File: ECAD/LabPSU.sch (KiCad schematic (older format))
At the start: 3 parts, among them J1 PWR

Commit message: work on things
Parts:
- removed D?: D_Bridge_+-AA, symbol Device:D_Bridge_+-AA
- added C? (x3): CP, symbol Device:CP
- added D1: FULL BRIDGE RECTIFIER, symbol Device:D_Bridge_+AA-
- added U?: BD9G341EFJ, Package_SO:HTSOP-8-1EP_3.9x4.9mm_P1.27mm_EP2.4x3.2mm_ThermalVias, symbol Regulator_Switching:BD9G341EFJ
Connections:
- net labels added: Earth, VDC
- wire segments 6 -> 15
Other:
- moved on the sheet: U?
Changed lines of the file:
@@
 	-1   0    0    1
-$EndComp
-$Comp
-L power:GND #PWR?
-U 1 1 61BA3EE6
-P 1950 2950
-F 0 "#PWR?" H 1950 2700 50  0001 C CNN
-F 1 "GND" H 1955 2777 50  0000 C CNN
-F 2 "" H 1950 2950 50  0001 C CNN
-F 3 "" H 1950 2950 50  0001 C CNN
-	1    1950 2950
-	1    0    0    -1
 $EndComp
 Wire Wire Line
 	1950 2950 1950 2850
-$Comp
-L power:VAC #PWR?
-U 1 1 61BA312C
-P 1950 2650
-F 0 "#PWR?" H 1950 2550 50  0001 C CNN
-F 1 "VAC" H 1950 2925 50  0000 C CNN
-F 2 "" H 1950 2650 50  0001 C CNN
-F 3 "" H 1950 2650 50  0001 C CNN
-	1    1950 2650
-	1    0    0    -1
-$EndComp
 Wire Wire Line
 	1900 2650 1950 2650
-$Comp
-L Device:D_Bridge_+-AA D?
-U 1 1 61BA4E82
-P 2700 2750
-F 0 "D?" H 3044 2796 50  0000 L CNN
-F 1 "D_Bridge_+-AA" H 3044 2705 50  0000 L CNN
-F 2 "" H 2700 2750 50  0001 C CNN
-F 3 "~" H 2700 2750 50  0001 C CNN
-	1    2700 2750
-	1    0    0    -1
-$EndComp
 Wire Wire Line
 	1900 2750 1950 2750
 Wire Wire Line
 	1950 2750 1950 2650
-Connection ~ 1950 2650
 Wire Wire Line
 	1950 2950 1900 2950
-Connection ~ 1950 2950
 Wire Wire Line
 	1900 2850 1950 2850
@@
 L Regulator_Switching:LM5118MH U?
 U 1 1 61BB989F
-P 4600 3400
-F 0 "U?" H 4600 4167 50  0000 C CNN
-F 1 "LM5118MH" H 4600 4076 50  0000 C CNN
-F 2 "Package_SO:Texas_PWP0020A" H 5300 4050 50  0001 L CNN
-F 3 "https://www.ti.com/lit/ds/symlink/lm5118.pdf" H 6600 2950 50  0001 C CNN
-	1    4600 3400
+P 4550 2500
+F 0 "U?" H 4550 3267 50  0000 C CNN
+F 1 "LM5118MH" H 4550 3176 50  0000 C CNN
+F 2 "Package_SO:Texas_PWP0020A" H 5250 3150 50  0001 L CNN
+F 3 "https://www.ti.com/lit/ds/symlink/lm5118.pdf" H 6550 2050 50  0001 C CNN
+	1    4550 2500
 	1    0    0    -1
 $EndComp
+$Comp
+L Regulator_Switching:BD9G341EFJ U?
+U 1 1 61BCA3CD
+P 4550 4350
+F 0 "U?" H 4550 5031 50  0000 C CNN
+F 1 "BD9G341EFJ" H 4550 4940 50  0000 C CNN
+F 2 "Package_SO:HTSOP-8-1EP_3.9x4.9mm_P1.27mm_EP2.4x3.2mm_ThermalVias" H 4650 3900 50  0001 L CNN
+F 3 "https://media.digikey.com/pdf/Data%20Sheets/Rohm%20PDFs/BD9G341EFJ.pdf" H 4550 4350 50  0001 C CNN
+	1    4550 4350
+	1    0    0    -1
+$EndComp
+$Comp
+L Device:D_Bridge_+AA- D1
+U 1 1 61BCBD61
+P 2600 2800
+F 0 "D1" H 2944 2846 50  0000 L CNN
+F 1 "FULL BRIDGE RECTIFIER" H 2150 2350 50  0000 L CNN
+F 2 "" H 2600 2800 50  0001 C CNN
+F 3 "~" H 2600 2800 50  0001 C CNN
+	1    2600 2800
+	1    0    0    -1
+$EndComp
+$Comp
+L power:VAC #PWR?
+U 1 1 61BCE152
+P 2150 2500
+F 0 "#PWR?" H 2150 2400 50  0001 C CNN
+F 1 "VAC" H 2150 2775 50  0000 C CNN
+F 2 "" H 2150 2500 50  0001 C CNN
+F 3 "" H 2150 2500 50  0001 C CNN
+	1    2150 2500
+	1    0    0    -1
+$EndComp
+Wire Wire Line
+	1950 2650 1950 2500
+Wire Wire Line
+	1950 2500 2150 2500
+Connection ~ 1950 2650
+Connection ~ 2150 2500
+Wire Wire Line
+	2150 2500 2600 2500
+Wire Wire Line
+	2600 3100 2150 3100
+Wire Wire Line
+	1950 3100 1950 2950
+Connection ~ 1950 2950
+$Comp
+L power:Earth #PWR?
+U 1 1 61BCF17A
+P 2150 3100
+F 0 "#PWR?" H 2150 2850 50  0001 C CNN
+F 1 "Earth" H 2150 2950 50  0001 C CNN
+F 2 "" H 2150 3100 50  0001 C CNN
+F 3 "~" H 2150 3100 50  0001 C CNN
+	1    2150 3100
+	1    0    0    -1
+$EndComp
+Connection ~ 2150 3100
+Wire Wire Line
+	2150 3100 1950 3100
+Wire Wire Line
+	2300 2800 2300 3200
+Wire Wire Line
+	2300 3200 3200 3200
+Wire Wire Line
+	2900 2800 3200 2800
+$Comp
+L power:VDC #PWR?
+U 1 1 61BD02AF
+P 3200 2800
+F 0 "#PWR?" H 3200 2700 50  0001 C CNN
+F 1 "VDC" H 3215 2973 50  0000 C CNN
+F 2 "" H 3200 2800 50  0001 C CNN
+F 3 "" H 3200 2800 50  0001 C CNN
+	1    3200 2800
+	1    0    0    -1
+$EndComp
+$Comp
+L power:GND #PWR?
+U 1 1 61BD0846
+P 3200 3200
+F 0 "#PWR?" H 3200 2950 50  0001 C CNN
+F 1 "GND" H 3205 3027 50  0000 C CNN
+F 2 "" H 3200 3200 50  0001 C CNN
+F 3 "" H 3200 3200 50  0001 C CNN
+	1    3200 3200
+	1    0    0    -1
+$EndComp
+$Comp
+L Device:CP C?
+U 1 1 61BD0AE5
+P 3000 3000
+F 0 "C?" H 3118 3046 50  0000 L CNN
+F 1 "CP" H 3118 2955 50  0000 L CNN
+F 2 "" H 3038 2850 50  0001 C CNN
+F 3 "~" H 3000 3000 50  0001 C CNN
+	1    3000 3000
+	1    0    0    -1
+$EndComp
+$Comp
+L Device:CP C?
+U 1 1 61BD13FA
+P 3350 3000
+F 0 "C?" H 3468 3046 50  0000 L CNN
+F 1 "CP" H 3468 2955 50  0000 L CNN
+F 2 "" H 3388 2850 50  0001 C CNN
+F 3 "~" H 3350 3000 50  0001 C CNN
+	1    3350 3000
+	1    0    0    -1
+$EndComp
+$Comp
+L Device:CP C?
+U 1 1 61BD178F
+P 3700 3000
+F 0 "C?" H 3818 3046 50  0000 L CNN
+F 1 "CP" H 3818 2955 50  0000 L CNN
+F 2 "" H 3738 2850 50  0001 C CNN
+F 3 "~" H 3700 3000 50  0001 C CNN
+	1    3700 3000
+	1    0    0    -1
+$EndComp

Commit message: Decided to remove AC/DC rectification
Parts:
- removed C? (x3): CP, symbol Device:CP
- removed D1: FULL BRIDGE RECTIFIER, symbol Device:D_Bridge_+AA-
- removed J1: PWR, symbol Connector:Screw_Terminal_01x04
- removed U?: BD9G341EFJ, Package_SO:HTSOP-8-1EP_3.9x4.9mm_P1.27mm_EP2.4x3.2mm_ThermalVias, symbol Regulator_Switching:BD9G341EFJ
- added C? (x5): 4.7uF, symbol Device:C
- added C?: 0.1uF, symbol Device:C
- added J1: PWR, symbol Connector:Screw_Terminal_01x02
- added R?: 1M, symbol Device:R
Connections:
- net labels added: VBUS
- net labels removed: Earth, VAC, VDC
- wire segments 15 -> 22
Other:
- note added: "DC Constant Regulated Input"
- note added: "Variable regulator"
- moved on the sheet: U?

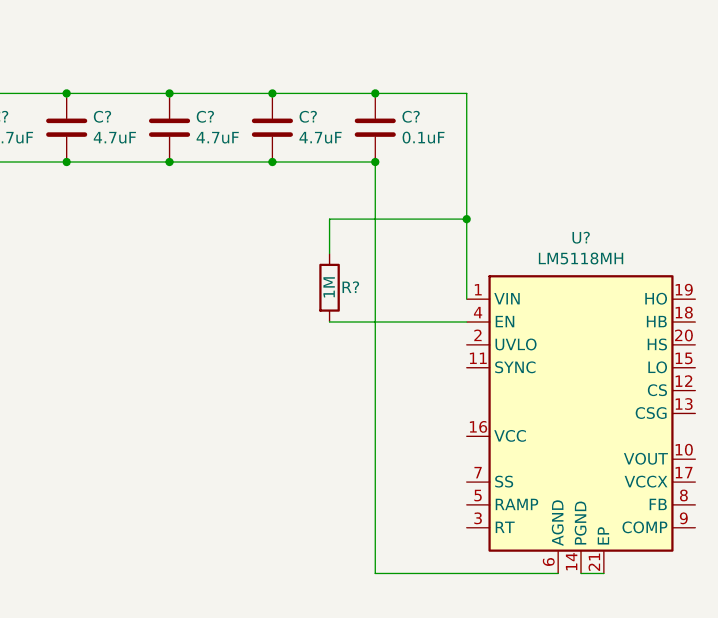
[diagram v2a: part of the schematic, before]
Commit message: add some extra circuitry to lm5118
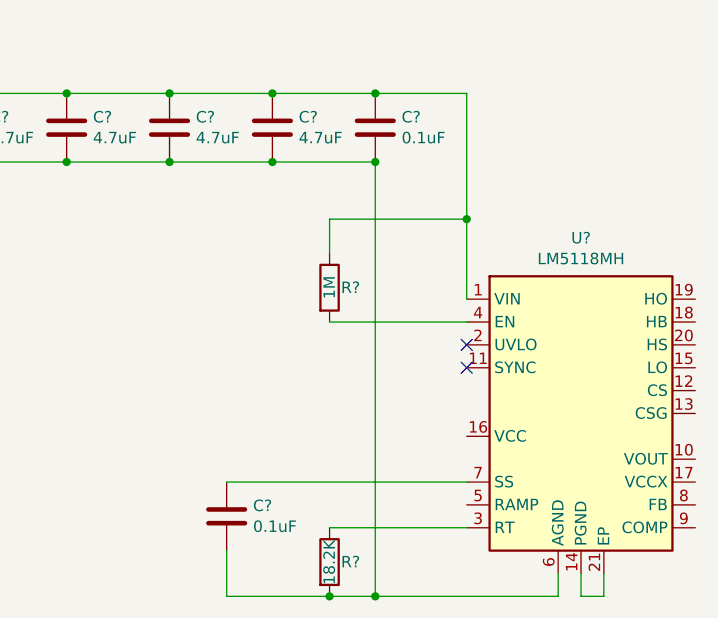
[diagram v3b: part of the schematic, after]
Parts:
- added C?: 0.1uF, symbol Device:C
- added R?: 18.2K, symbol Device:R
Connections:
- net at U?.3 (RT): now also R?.1
- net at C?.2, C?.2, C?.2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: now also C?.2, R?.2
- net at U?.7 (SS): now also C?.1
- no-connect marks 0 -> 2
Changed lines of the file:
@@
 Connection ~ 4200 2050
 Wire Wire Line
-	4650 3850 5450 3850
-Wire Wire Line
-	5550 3850 5650 3850
+	4650 3950 5450 3950
 $Comp
 L Regulator_Switching:LM5118MH U?
@@
 	1    0    0    -1
 $EndComp
-Wire Wire Line
-	4650 2050 4650 3850
 Connection ~ 4650 2050
 Wire Wire Line
@@
 Text Notes 5200 1300 0    50   ~ 0
 Variable regulator
+$Comp
+L Device:R R?
+U 1 1 61C0F85E
+P 4450 3800
+F 0 "R?" H 4500 3800 50  0000 L CNN
+F 1 "18.2K" V 4450 3700 50  0000 L CNN
+F 2 "" V 4380 3800 50  0001 C CNN
+F 3 "~" H 4450 3800 50  0001 C CNN
+	1    4450 3800
+	1    0    0    -1
+$EndComp
+Wire Wire Line
+	4450 3650 5050 3650
+Wire Wire Line
+	5450 3950 5450 3850
+Wire Wire Line
+	4650 2050 4650 3950
+Wire Wire Line
+	4450 3950 4650 3950
+Connection ~ 4650 3950
+Wire Wire Line
+	5550 3850 5550 3950
+Wire Wire Line
+	5550 3950 5650 3950
+Wire Wire Line
+	5650 3950 5650 3850
+$Comp
+L Device:C C?
+U 1 1 61C13AAB
+P 4000 3600
+F 0 "C?" H 4115 3646 50  0000 L CNN
+F 1 "0.1uF" H 4115 3555 50  0000 L CNN
+F 2 "" H 4038 3450 50  0001 C CNN
+F 3 "~" H 4000 3600 50  0001 C CNN
+	1    4000 3600
+	1    0    0    -1
+$EndComp
+Wire Wire Line
+	4000 3450 5050 3450
+Wire Wire Line
+	4000 3750 4000 3950
+Wire Wire Line
+	4000 3950 4450 3950
+Connection ~ 4450 3950
+NoConn ~ 5050 2950
+NoConn ~ 5050 2850
 $EndSCHEMATC

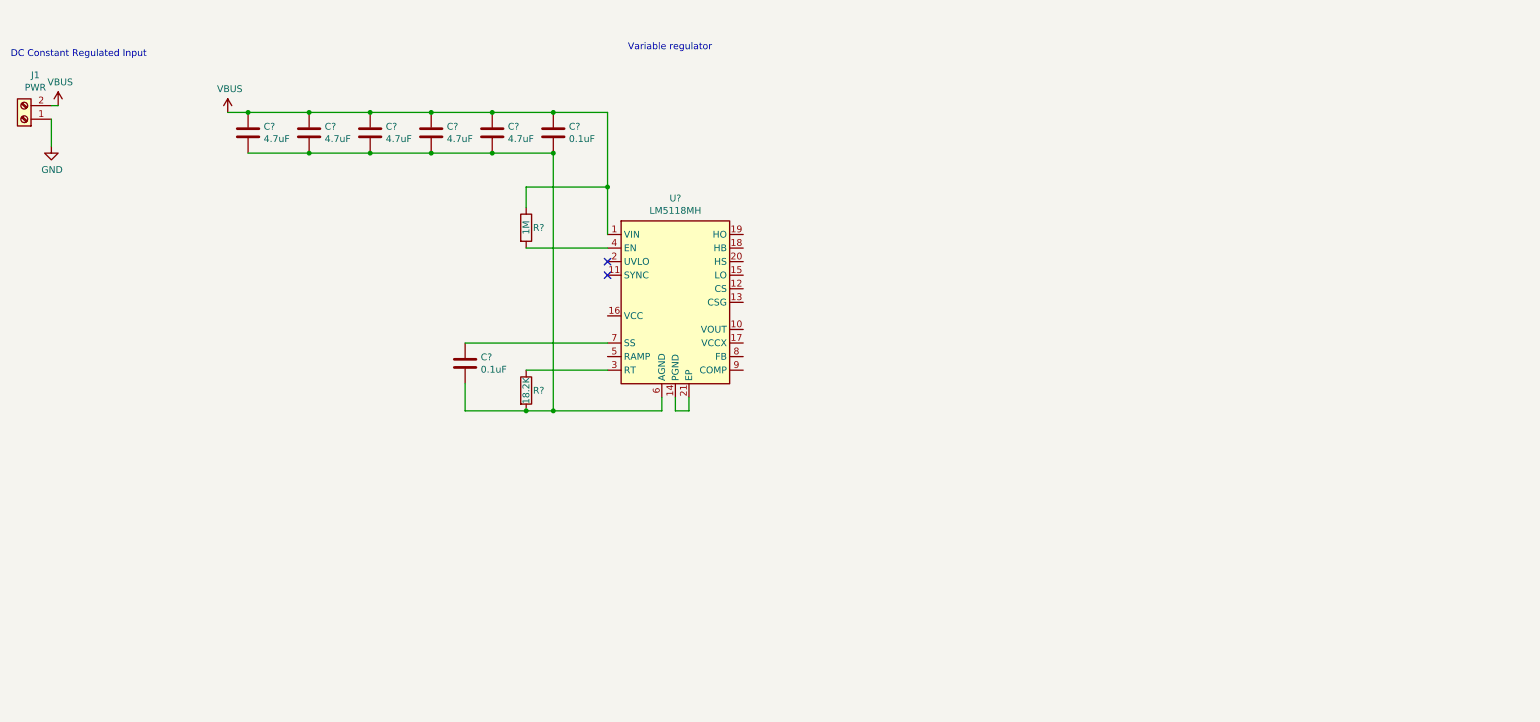
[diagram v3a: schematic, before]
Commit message: Finish adding lm5118 components, yet to calculate values
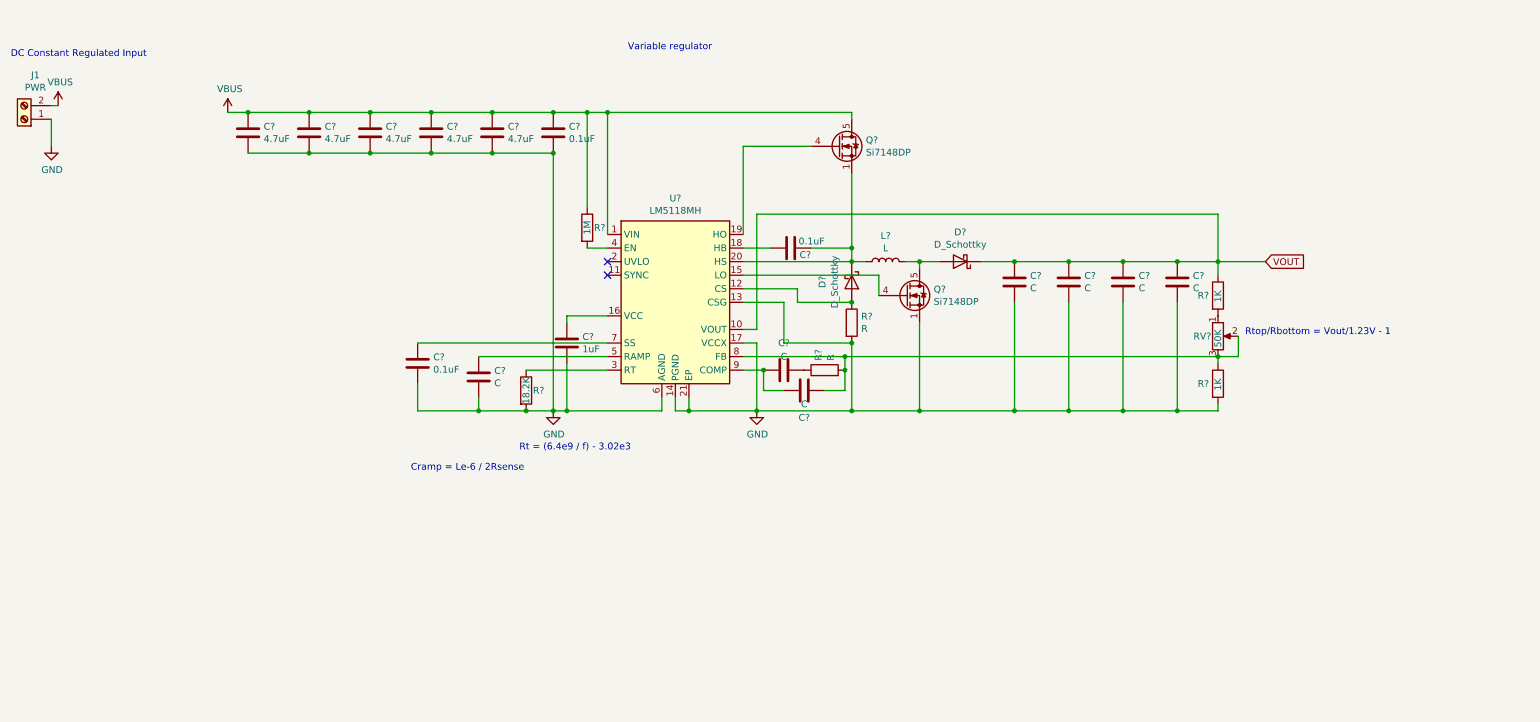
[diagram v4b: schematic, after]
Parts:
- added C? (x7): C, symbol Device:C
- added C?: 1uF, symbol Device:C
- added C?: 0.1uF, symbol Device:C
- added D? (x2): D_Schottky, symbol Device:D_Schottky
- added L?: L, symbol Device:L
- added Q? (x2): Si7148DP, Package_SO:PowerPAK_SO-8_Single, symbol Transistor_FET:Si7336ADP
- added R? (x2): R, symbol Device:R
- added R? (x2): 1K, symbol Device:R
- added RV?: 50K, symbol Device:R_POT
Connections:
- net GND: now also C?.2, C?.2, C?.2, C?.2, C?.2, C?.2, C?.2, R?.2, U?.13 (CSG), U?.14 (PGND), U?.17 (VCCX), U?.21 (EP), U?.6 (AGND), C?.2, C?.2, C?.2, C?.2, C?.2, C?.2, Q?.1 (S), Q?.2 (S), Q?.3 (S), R?.2, R?.2
- net VBUS: now also Q?.5 (D)
- net VOUT: now reaches U?.10 (VOUT)
- net VOUT: now also C?.1, C?.1, C?.1, C?.1, D?.1 (K), R?.1
- net at U?.12 (CS): now also D?.2 (A), R?.1
- net at U?.15 (LO): now also Q?.4 (G)
- net at U?.16 (VCC): now also C?.1
- net at U?.18 (HB): now also C?.1
- net at U?.19 (HO): now also Q?.4 (G)
- net at U?.20 (HS): now also C?.2, D?.1 (K), L?.1, Q?.1 (S), Q?.2 (S), Q?.3 (S)
- net at U?.5 (RAMP): now also C?.1
- net at U?.8 (FB): now also C?.1, R?.1, R?.2, RV?.2, RV?.3
- net at U?.9 (COMP): now also C?.2, C?.2
- new net: D?.2 (A), L?.2, Q?.5 (D)
- new net: C?.1, R?.1
- new net: R?.2, RV?.1
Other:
- note added: "Cramp = Le-6 / 2Rsense"
- note added: "Rt = (6.4e9 / f) - 3.02e3"
- note added: "Rtop/Rbottom = Vout/1.23V - 1"
- moved on the sheet: C?, R?

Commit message: add fixed buck regulator
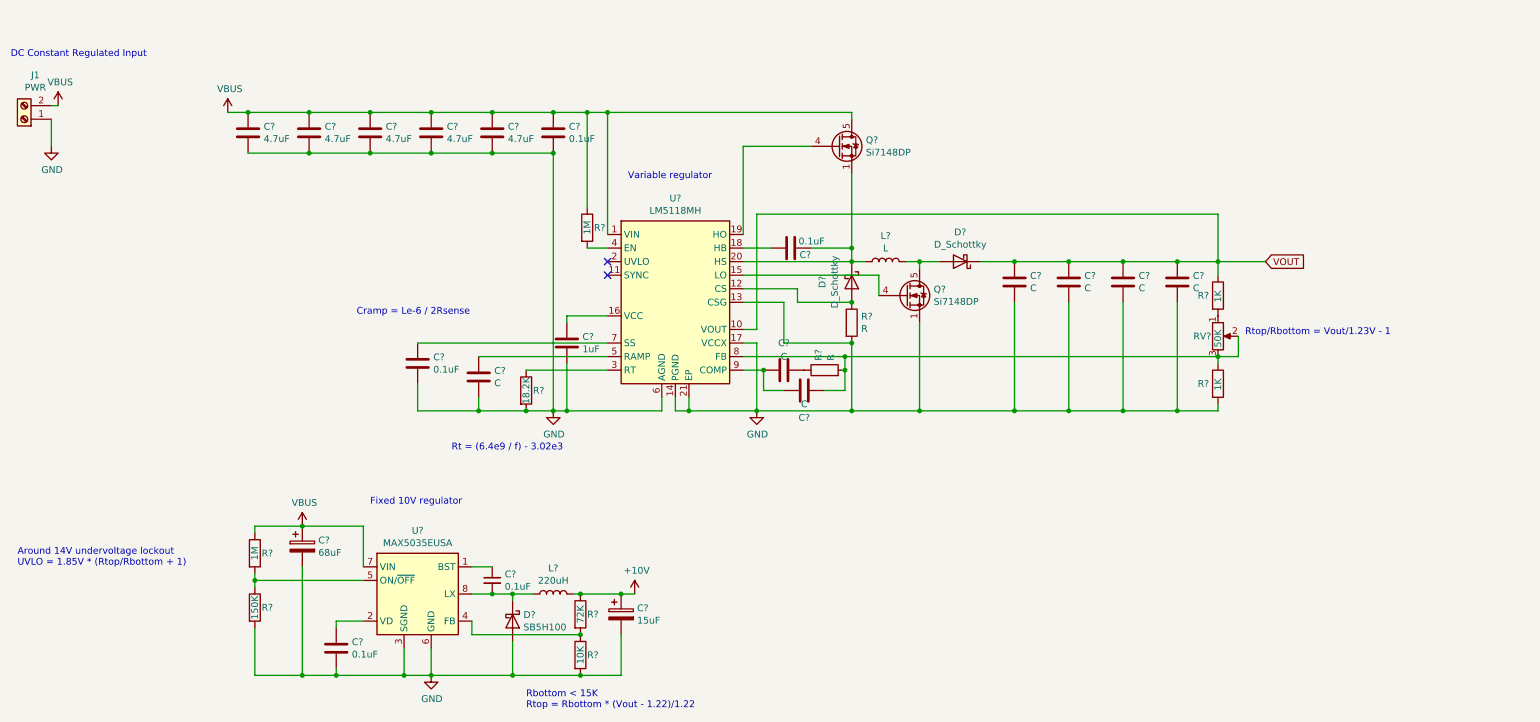
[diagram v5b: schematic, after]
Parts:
- added C?: 68uF, symbol Device:CP
- added C?: 0.1uF, symbol Device:C
- added C?: 0.1uF, symbol Device:C_Small
- added C?: 15uF, symbol Device:CP
- added D?: SB5H100, symbol Device:D_Schottky
- added L?: 220uH, symbol Device:L
- added R?: 150K, symbol Device:R
- added R?: 1M, symbol Device:R
- added R?: 72K, symbol Device:R
- added R?: 10K, symbol Device:R
- added U?: MAX5035EUSA, Package_SO:SOIC-8_3.9x4.9mm_P1.27mm, symbol Regulator_Switching:MAX5035EUSA
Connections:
- net GND: now also C?.2, C?.2, C?.2, D?.2 (A), R?.2, R?.2, U?.3 (SGND), U?.6 (GND)
- net VBUS: now also C?.1, R?.1, U?.7 (VIN)
- new net: C?.1, U?.1 (BST)
- new net: C?.1, U?.2 (VD)
- new net: R?.1, R?.2, U?.4 (FB)
- new net: R?.1, R?.2, U?.5 (ON/~OFF~)
- new net: C?.2, D?.1 (K), L?.1, U?.8 (LX)
- new net +10V: C?.1, L?.2, R?.1
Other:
- note added: "Around 14V undervoltage lockout\nUVLO = 1.85V * (Rtop/Rbottom + 1)"
- note added: "Fixed 10V regulator"
- note added: "Rbottom < 15K\nRtop = Rbottom * (Vout - 1.22)/1.22"

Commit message: end of day commit
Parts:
- added R?: 10m, symbol Device:R
- added U?: LT6106, Package_TO_SOT_SMD:SOT-23-5, symbol Amplifier_Current:LT6106
- added U?: AD5272BRM, Package_SO:MSOP-10_3x3mm_P0.5mm, symbol Potentiometer_Digital:AD5272BRM
- added U?: MCP4811, symbol Analog_DAC:MCP4811
- L?: value L -> 300uH
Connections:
- net VOUT: now also R?.1; no longer C?.1, C?.1, C?.1, C?.1, D?.1 (K), R?.1, U?.10 (VOUT)
- new net: C?.1, C?.1, C?.1, C?.1, D?.1 (K), R?.1, R?.2, U?.10 (VOUT)
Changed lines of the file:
@@
 P 7100 2850
 F 0 "L?" V 7290 2850 50  0000 C CNN
-F 1 "L" V 7199 2850 50  0000 C CNN
+F 1 "300uH" V 7199 2850 50  0000 C CNN
 F 2 "" H 7100 2850 50  0001 C CNN
 F 3 "~" H 7100 2850 50  0001 C CNN
@@
 	1    0    0    -1
 $EndComp
-Text GLabel 9900 2850 2    50   Input ~ 0
+Text GLabel 10100 2850 2    50   Input ~ 0
 VOUT
-Wire Wire Line
-	9550 2850 9900 2850
 Text Notes 9750 3400 0    50   ~ 0
 Rtop/Rbottom = Vout/1.23V - 1
@@
 Text Notes 3300 4650 0    50   ~ 0
 Fixed 10V regulator
+$Comp
+L Device:R R?
+U 1 1 61C130DF
+P 9850 2850
+F 0 "R?" V 9750 2850 50  0000 C CNN
+F 1 "10m" V 9850 2850 50  0000 C CNN
+F 2 "" V 9780 2850 50  0001 C CNN
+F 3 "~" H 9850 2850 50  0001 C CNN
+	1    9850 2850
+	0    1    1    0
+$EndComp
+Wire Wire Line
+	9700 2850 9550 2850
+Wire Wire Line
+	10100 2850 10000 2850
+$Comp
+L Amplifier_Current:LT6106 U?
+U 1 1 61C2B752
+P 10350 2300
+F 0 "U?" H 10694 2346 50  0000 L CNN
+F 1 "LT6106" H 10694 2255 50  0000 L CNN
+F 2 "Package_TO_SOT_SMD:SOT-23-5" H 10350 2300 50  0001 C CNN
+F 3 "https://www.analog.com/media/en/technical-documentation/data-sheets/6106fb.pdf" H 10400 2500 50  0001 C CNN
+	1    10350 2300
+	1    0    0    -1
+$EndComp
+$Comp
+L Potentiometer_Digital:AD5272BRM U?
+U 1 1 61C321DA
+P 11250 4150
+F 0 "U?" H 11250 4831 50  0000 C CNN
+F 1 "AD5272BRM" H 11250 4740 50  0000 C CNN
+F 2 "Package_SO:MSOP-10_3x3mm_P0.5mm" H 12000 3700 50  0001 C CNN
+F 3 "https://www.analog.com/media/en/technical-documentation/data-sheets/AD5272_5274.pdf" H 11250 4150 50  0001 C CNN
+	1    11250 4150
+	1    0    0    -1
+$EndComp
+$Comp
+L Analog_DAC:MCP4811 U?
+U 1 1 61C336A7
+P 9400 1400
+F 0 "U?" H 10044 1446 50  0000 L CNN
+F 1 "MCP4811" H 10044 1355 50  0000 L CNN
+F 2 "" H 10300 1300 50  0001 C CNN
+F 3 "http://ww1.microchip.com/downloads/en/DeviceDoc/22244B.pdf" H 10300 1300 50  0001 C CNN
+	1    9400 1400
+	1    0    0    -1
+$EndComp
 $EndSCHEMATC
